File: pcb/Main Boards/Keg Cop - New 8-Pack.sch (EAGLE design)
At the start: 15 parts, among them X1 RJ45-8X, X2 RJ45-8X

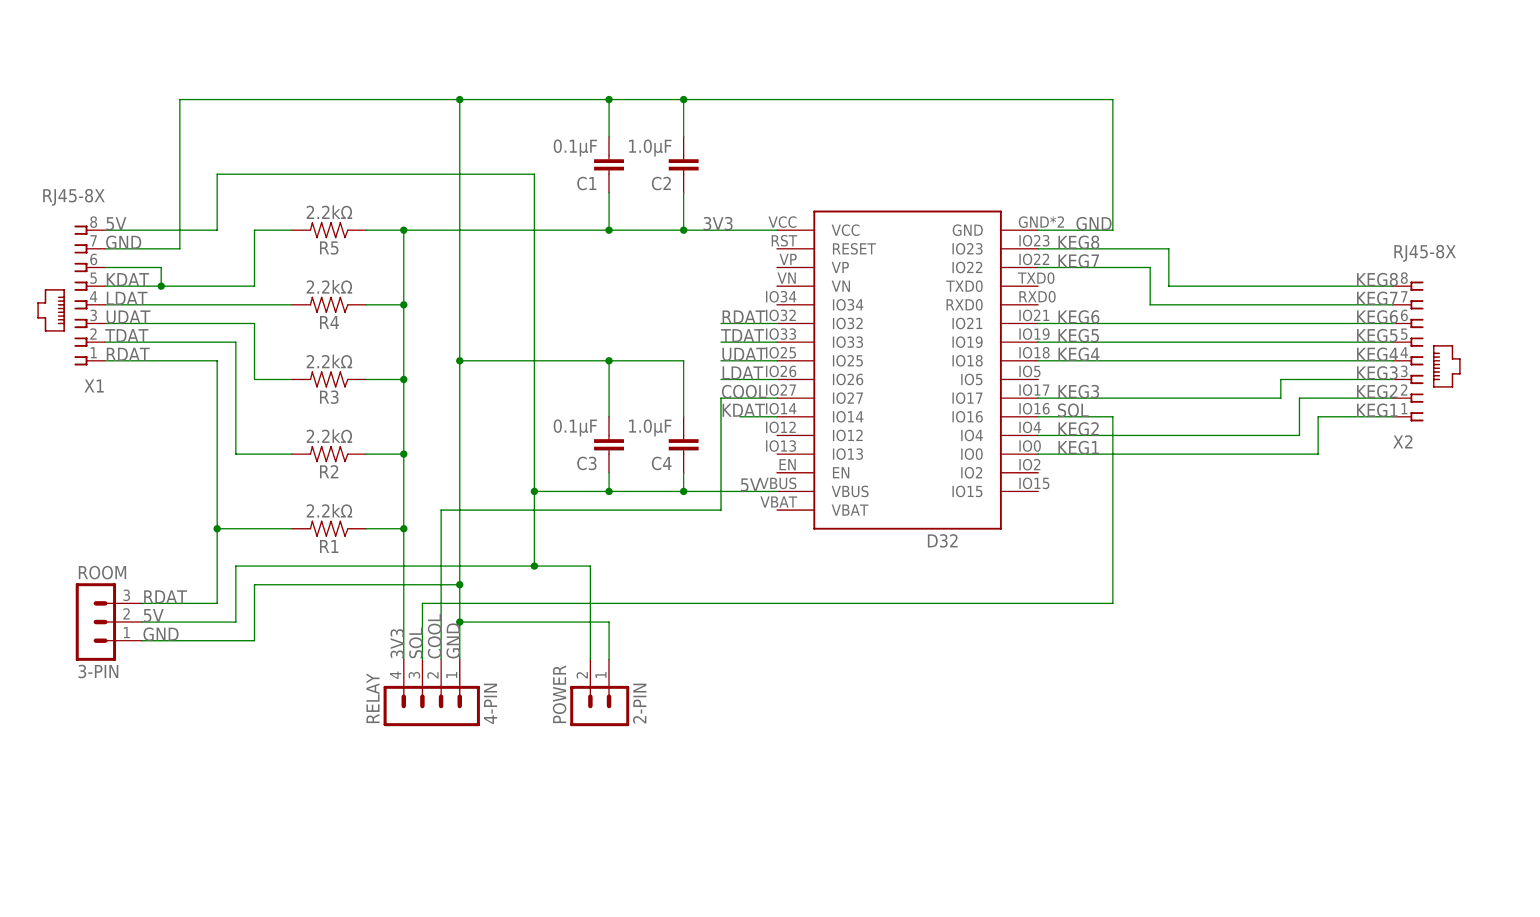
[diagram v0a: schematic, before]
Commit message: Begin new board for 8 flowmeters
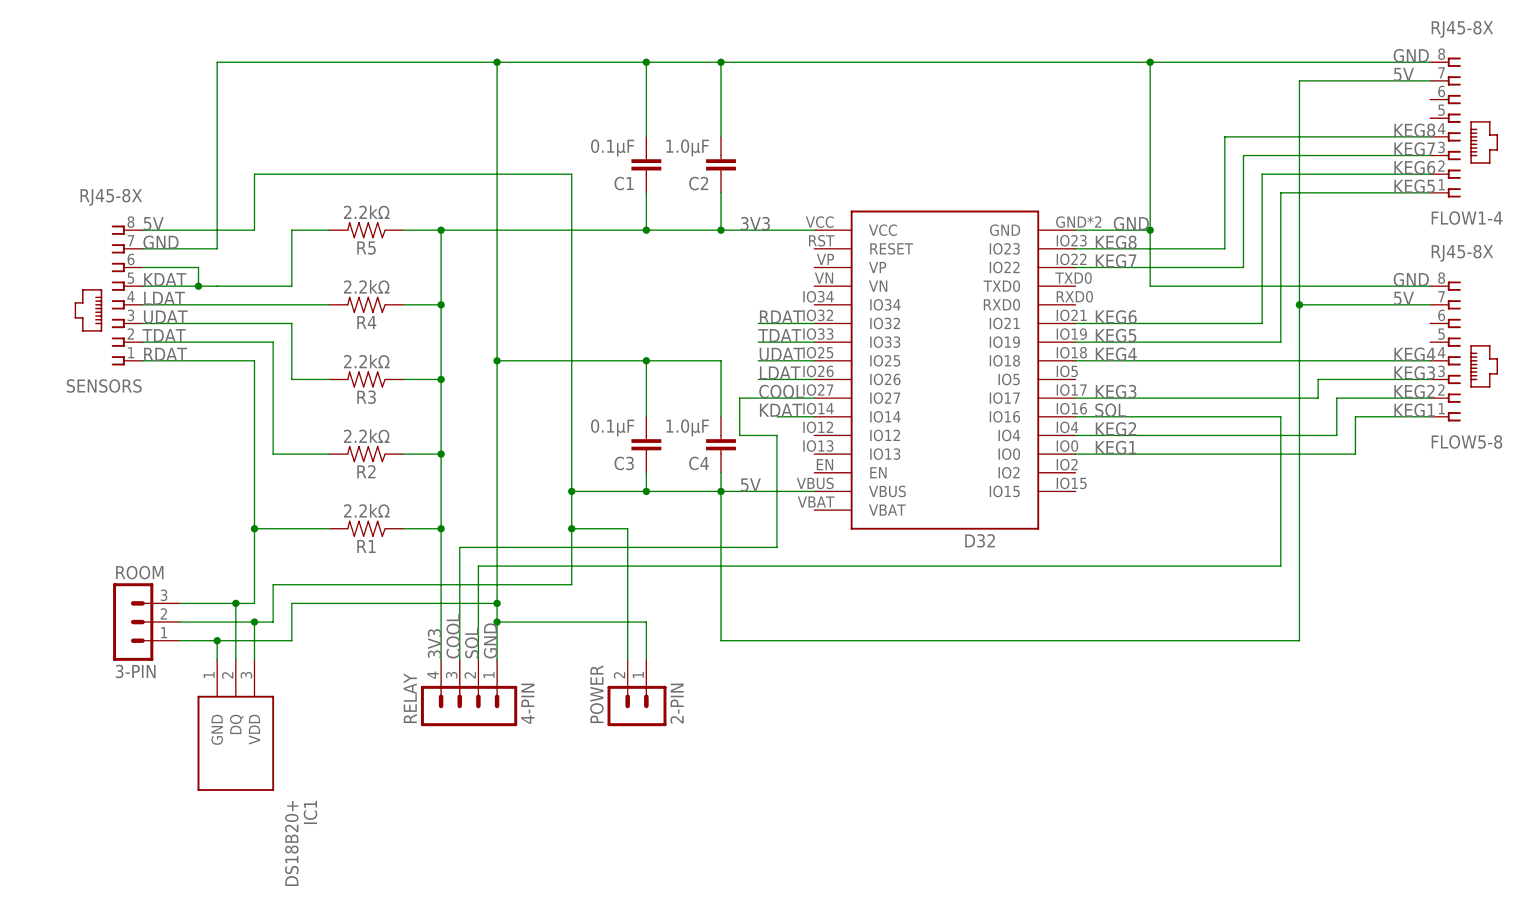
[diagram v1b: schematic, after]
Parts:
- removed X1, X2: RJ45-8X, con-tycoelectronics:RJ45-8X
- added FLOW1-4, FLOW5-8, SENSORS: RJ45-8X, con-tycoelectronics:RJ45-8X
- added IC1: DS18B20+, SamacSys_Parts:DS18B20+
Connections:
- net 5V: now also FLOW1-4.7, FLOW5-8.7, IC1.VDD, SENSORS.8; no longer X1.8
- net COOL: now also RELAY.3; no longer RELAY.2
- net GND: now also FLOW1-4.8, FLOW5-8.8, IC1.GND, SENSORS.7; no longer X1.7
- net KDAT: now also SENSORS.5, SENSORS.6; no longer X1.5, X1.6
- net KEG1: now also FLOW5-8.1; no longer X2.1
- net KEG2: now also FLOW5-8.2; no longer X2.2
- net KEG3: now also FLOW5-8.3; no longer X2.3
- net KEG4: now also FLOW5-8.4; no longer X2.4
- net KEG5: now also FLOW1-4.1; no longer X2.5
- net KEG6: now also FLOW1-4.2; no longer X2.6
- net KEG7: now also FLOW1-4.3; no longer X2.7
- net KEG8: now also FLOW1-4.4; no longer X2.8
- net LDAT: now also SENSORS.4; no longer X1.4
- net RDAT: now also IC1.DQ, SENSORS.1; no longer X1.1
- net SOL: now also RELAY.2; no longer RELAY.3
- net TDAT: now also SENSORS.2; no longer X1.2
- net UDAT: now also SENSORS.3; no longer X1.3
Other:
- moved on the sheet: C1, C2, C3, C4, D32, POWER, R1, R2, R3, R4, R5, RELAY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
